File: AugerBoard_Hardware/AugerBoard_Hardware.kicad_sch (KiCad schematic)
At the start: 48 parts, among them J1 RJ45_LED_Shielded, SW1 SW_SPDT, SW2 SW_Push, SW3 SW_Push, SW4 SW_Push, SW5 SW_Push, U1 Teensy4.1_DEV-16771, U2 OKI-78SR-5_1.5-W36H-C

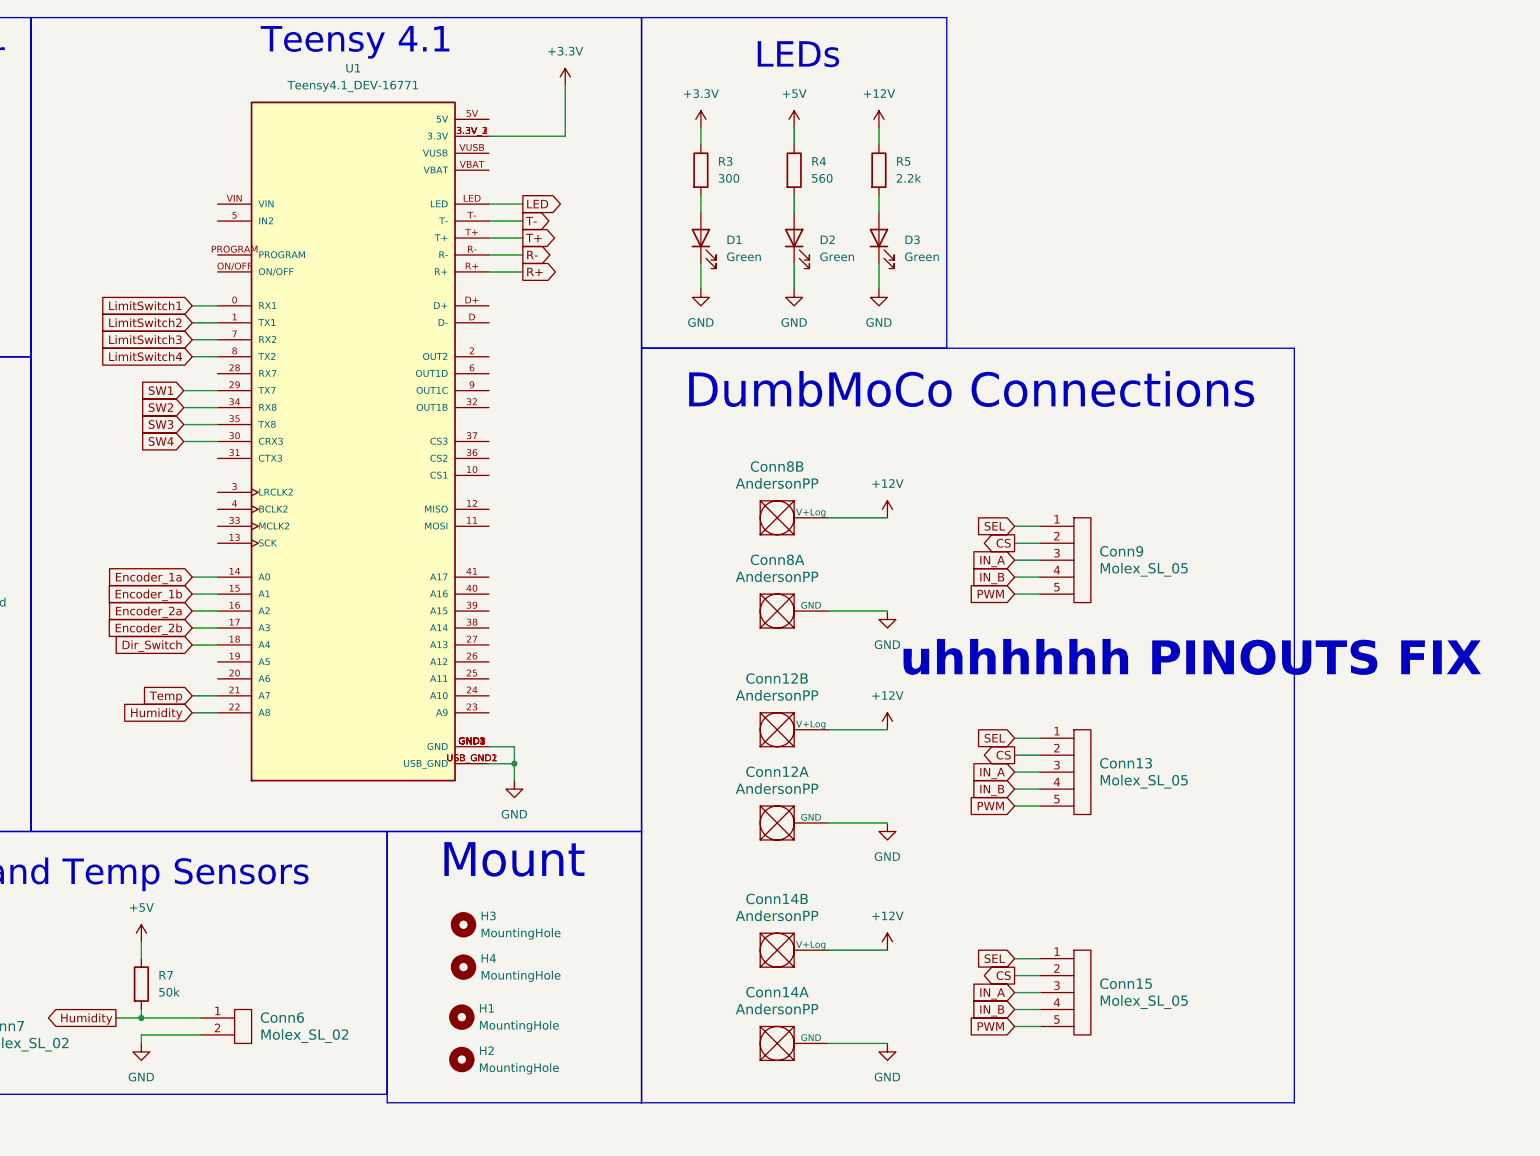
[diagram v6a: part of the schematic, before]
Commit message: Fixed and double checked all pin connections to the teensy
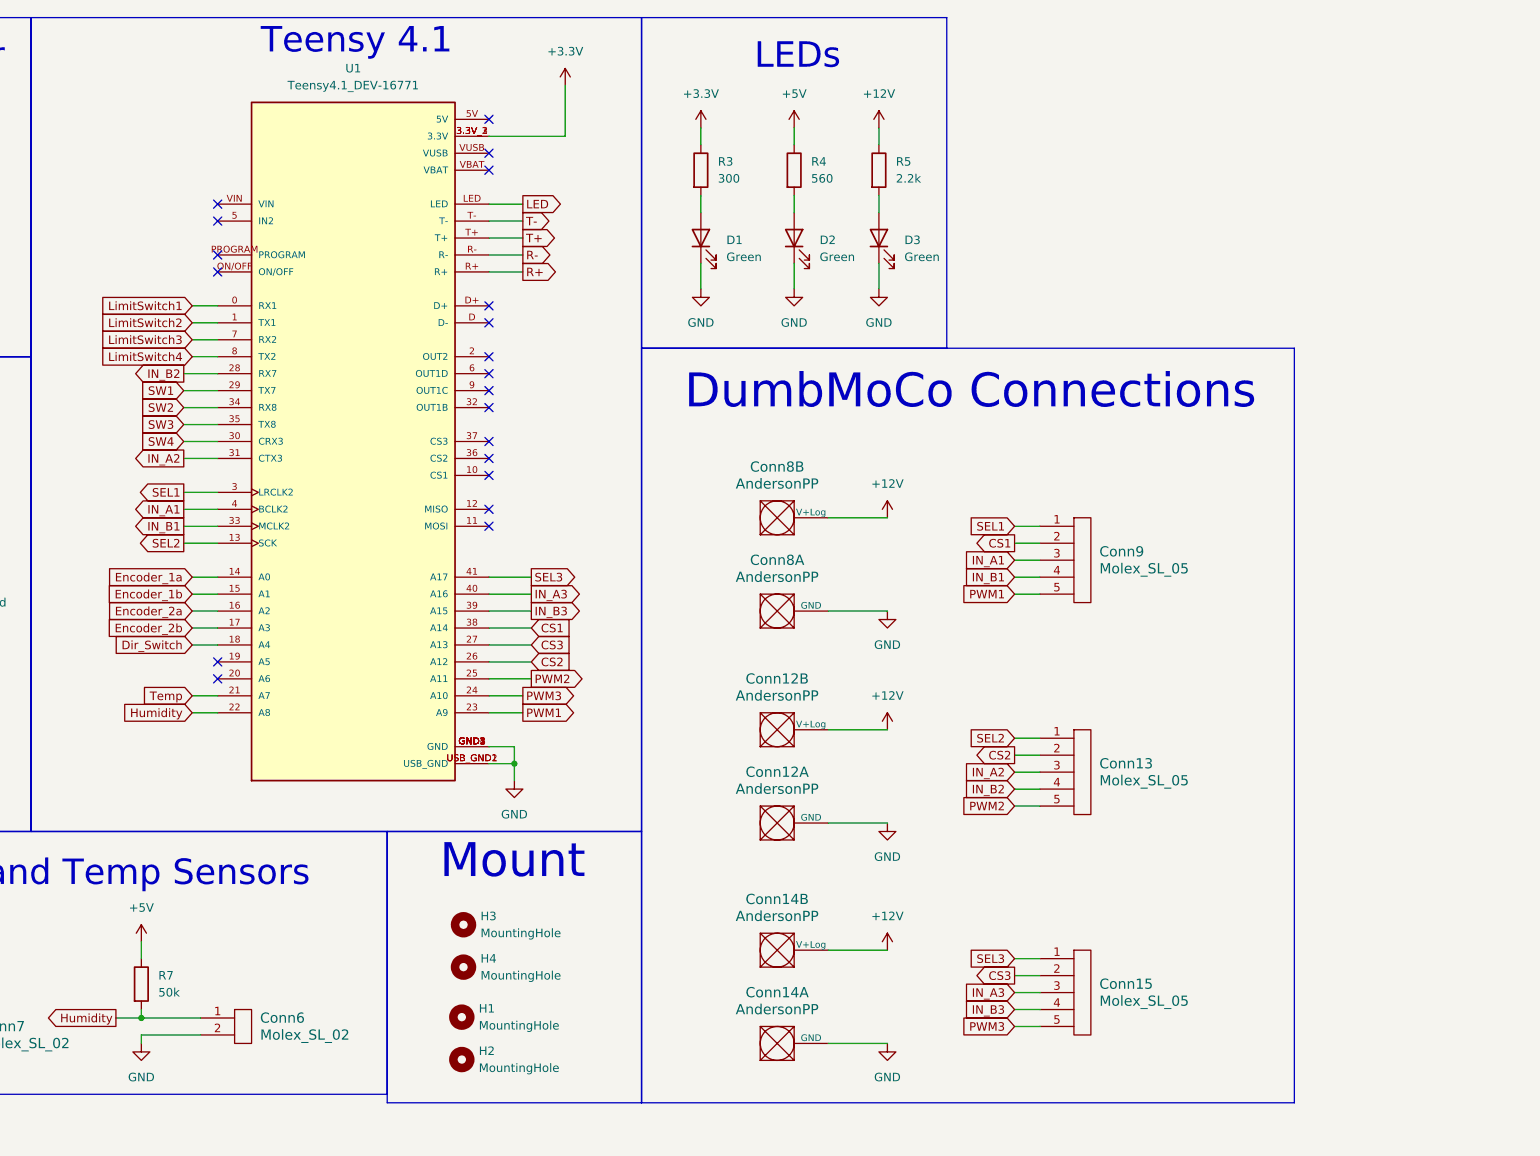
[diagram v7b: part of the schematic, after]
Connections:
- net SEL2: now reaches U1.13 (SCK)
- net SEL2: now also Conn13.1
- net PWM1: now reaches U1.23 (A9)
- net PWM1: now also Conn9.5
- net PWM3: now reaches U1.24 (A10)
- net PWM3: now also Conn15.5
- net PWM2: now reaches U1.25 (A11)
- net PWM2: now also Conn13.5
- net CS2: now reaches U1.26 (A12)
- net CS2: now also Conn13.2
- net CS3: now reaches U1.27 (A13)
- net CS3: now also Conn15.2
- net IN_B2: now reaches U1.28 (RX7)
- net IN_B2: now also Conn13.4
- net SEL1: now reaches U1.3 (LRCLK2)
- net SEL1: now also Conn9.1
- net IN_A2: now reaches U1.31 (CTX3)
- net IN_A2: now also Conn13.3
- net IN_B1: now reaches U1.33 (MCLK2)
- net IN_B1: now also Conn9.4
- net CS1: now reaches U1.38 (A14)
- net CS1: now also Conn9.2
- net IN_B3: now reaches U1.39 (A15)
- net IN_B3: now also Conn15.4
- net IN_A1: now reaches U1.4 (BCLK2)
- net IN_A1: now also Conn9.3
- net IN_A3: now reaches U1.40 (A16)
- net IN_A3: now also Conn15.3
- net SEL3: now reaches U1.41 (A17)
- net SEL3: now also Conn15.1
- removed net CS: Conn13.2, Conn15.2, Conn9.2
- removed net IN_A: Conn13.3, Conn15.3, Conn9.3
- removed net IN_B: Conn13.4, Conn15.4, Conn9.4
- removed net PWM: Conn13.5, Conn15.5, Conn9.5
- removed net SEL: Conn13.1, Conn15.1, Conn9.1
- no-connect marks 3 -> 23
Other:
- note removed: "uhhhhhh PINOUTS FIX"

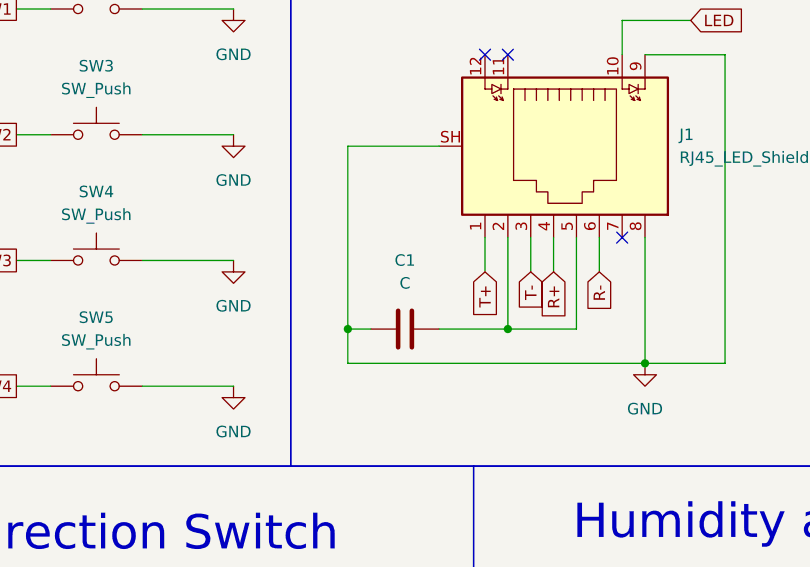
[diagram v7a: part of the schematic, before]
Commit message: Fixed a capacitor value
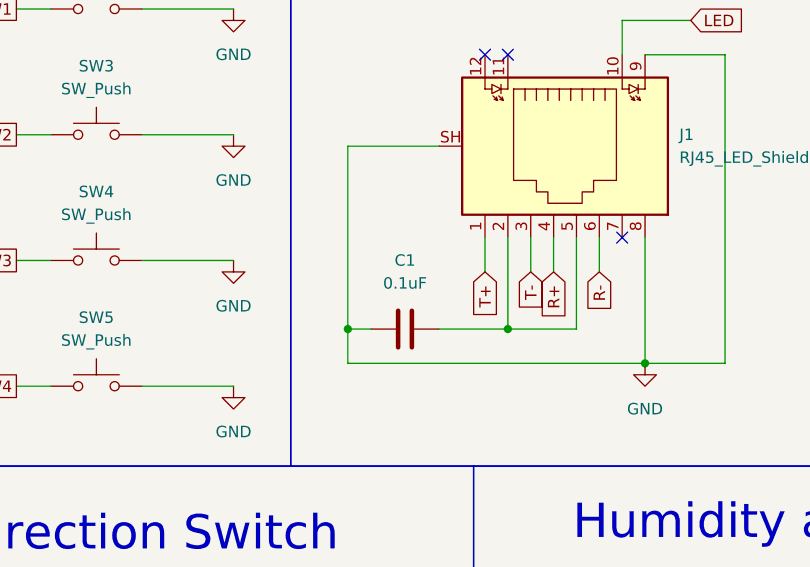
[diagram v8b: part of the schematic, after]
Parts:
- C1: value C -> 0.1uF
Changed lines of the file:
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@@
 			)
 		)
-		(property "Value" "C"
+		(property "Value" "0.1uF"
 			(at 146.05 115.57 90)
 			(effects
